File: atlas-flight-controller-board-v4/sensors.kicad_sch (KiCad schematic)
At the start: 14 parts, among them IC1 LSM6DSV80XTR, U2 LIS2MDL, U3 SAM-M10Q-00B

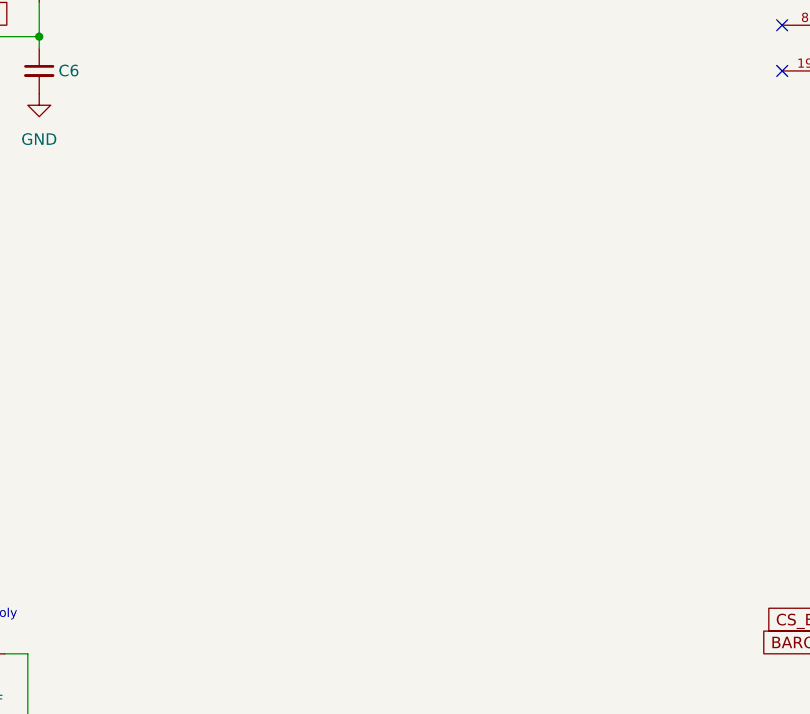
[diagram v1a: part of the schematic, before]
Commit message: commiting files to v10 branch. Only v9 is working well on linux so seperating to reduce headache while sorting out issues
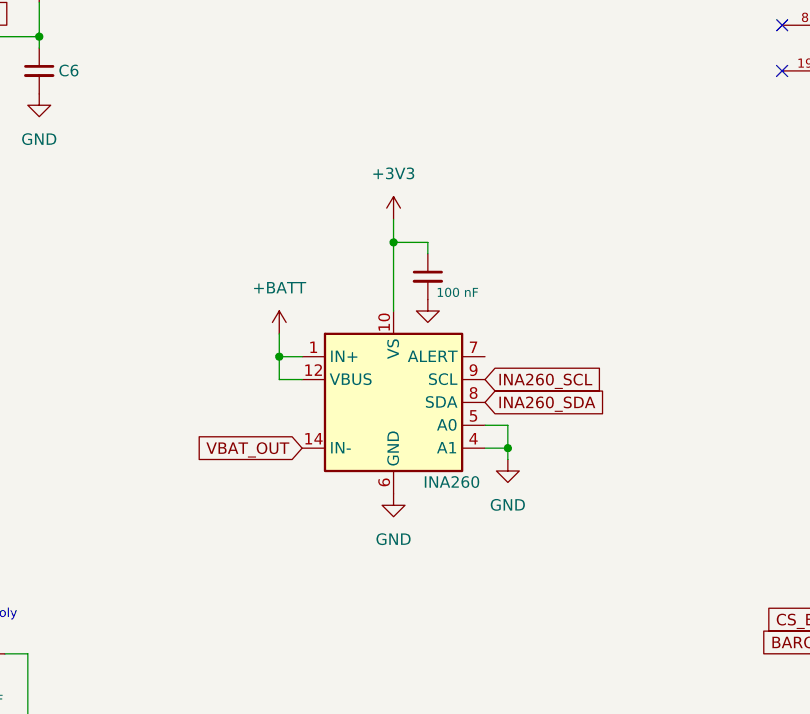
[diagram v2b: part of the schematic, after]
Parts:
- added C27: 100 nF, Capacitor_SMD:C_0603_1608Metric_Pad1.08x0.95mm_HandSolder, symbol Device:C_Small
- added U5: INA260, Package_SO:TSSOP-16_4.4x5mm_P0.65mm, symbol Sensor_Energy:INA260
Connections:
- net +3V3: now also C27.1, U5.10 (VS)
- net GND: now also C27.2, U5.11 (GND), U5.4 (A1), U5.5 (A0), U5.6 (GND)
- new net +BATT: U5.1 (IN+), U5.12 (VBUS), U5.2 (IN+), U5.3 (IN+)
- new net INA260_SCL: U5.9 (SCL)
- new net INA260_SDA: U5.8 (SDA)
- new net VBAT_OUT: U5.14 (IN-), U5.15 (IN-), U5.16 (IN-)

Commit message: wip commit, hopefully last from mac
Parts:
- removed C1: 10 uF, CAP_APA_0606_AVX, symbol APA0606100M050R:_1
- added C43: 10uF, Capacitor_SMD:C_0603_1608Metric, symbol Device:C_Small
- C10, C27, C5, C6, C7, C8, C9: footprint Capacitor_SMD:C_0603_1608Metric_Pad1.08x0.95mm_HandSolder -> Capacitor_SMD:C_0603_1608Metric
- C2, C3: value 100 nF -> 100nF; footprint Capacitor_SMD:C_0603_1608Metric_Pad1.08x0.95mm_HandSolder -> Capacitor_SMD:C_0603_1608Metric
- C4: value 220 nF -> 220nF; footprint Capacitor_SMD:C_0603_1608Metric_Pad1.08x0.95mm_HandSolder -> Capacitor_SMD:C_0603_1608Metric
- U2: footprint LIS2MDL:PQFN50P200X200X70-12N -> Package_LGA:LGA-12_2x2mm_P0.5mm
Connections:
- net +3V3: now also C43.2
- net GND: now also C43.1
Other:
- note removed: "Alum Poly"
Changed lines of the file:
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@@
 	(generator_version "10.0")
 	(paper "A4")
-	(text "Alum Poly\n"
-		(exclude_from_sim no)
-		(at 99.568 127.762 0)
-		(effects
-			(font
-				(size 1 1)
-			)
-		)
-	)
 	(junction
 		(at 76.2 81.28)
@@
 	(wire
 		(pts
-			(xy 49.53 160.02) (xy 50.8 160.02)
-		)
-		(stroke
-			(width 0)
-			(type default)
-		)
-	)
-	(wire
-		(pts
 			(xy 39.37 62.23) (xy 39.37 60.96)
 		)
@@
 	(wire
 		(pts
-			(xy 49.53 157.48) (xy 50.8 157.48)
-		)
-		(stroke
-			(width 0)
-			(type default)
-		)
-	)
-	(wire
-		(pts
 			(xy 246.38 130.81) (xy 250.19 130.81)
 		)
@@
 	(wire
 		(pts
-			(xy 49.53 152.4) (xy 50.8 152.4)
-		)
-		(stroke
-			(width 0)
-			(type default)
-		)
-	)
-	(wire
-		(pts
 			(xy 95.25 132.08) (xy 96.52 132.08)
 		)
@@
 	(global_label "SCK_MEMS"
 		(shape input)
-		(at 49.53 152.4 180)
+		(at 50.8 152.4 180)
 		(fields_autoplaced yes)
 		(effects
@@
 		)
 		(property "Intersheetrefs" "${INTERSHEET_REFS}"
-			(at 36.5664 152.4 0)
+			(at 37.8364 152.4 0)
 			(hide yes)
 			(show_name no)
@@
 	(global_label "MISO_MEMS"
 		(shape input)
-		(at 49.53 160.02 180)
+		(at 50.8 160.02 180)
 		(fields_autoplaced yes)
 		(effects
@@
 		)
 		(property "Intersheetrefs" "${INTERSHEET_REFS}"
-			(at 35.7197 160.02 0)
+			(at 36.9897 160.02 0)
 			(hide yes)
 			(show_name no)
@@
 	(global_label "MOSI_MEMS"
 		(shape input)
-		(at 49.53 157.48 180)
+		(at 50.8 157.48 180)
 		(fields_autoplaced yes)
 		(effects
@@
 		)
 		(property "Intersheetrefs" "${INTERSHEET_REFS}"
-			(at 35.7197 157.48 0)
+			(at 36.9897 157.48 0)
 			(hide yes)
 			(show_name no)
@@
 			)
 		)
-		(property "Value" "100 nF"
+		(property "Value" "100nF"
 			(at 99.06 137.16 90)
 			(show_name no)
@@
 			)
 		)
-		(property "Footprint" "Capacitor_SMD:C_0603_1608Metric_Pad1.08x0.95mm_HandSolder"
+		(property "Footprint" "Capacitor_SMD:C_0603_1608Metric"
 			(at 99.06 139.7 0)
 			(hide yes)
@@
 			)
 		)
-		(property "Footprint" "Capacitor_SMD:C_0603_1608Metric_Pad1.08x0.95mm_HandSolder"
+		(property "Footprint" "Capacitor_SMD:C_0603_1608Metric"
 			(at 243.84 124.46 0)
 			(hide yes)
@@
 			)
 		)
-		(property "Footprint" "Capacitor_SMD:C_0603_1608Metric_Pad1.08x0.95mm_HandSolder"
+		(property "Footprint" "Capacitor_SMD:C_0603_1608Metric"
 			(at 238.76 52.07 0)
 			(hide yes)
@@
 			)
 		)
-		(property "Value" "100 nF"
+		(property "Value" "100nF"
 			(at 99.314 144.78 90)
 			(show_name no)
@@
 			)
 		)
-		(property "Footprint" "Capacitor_SMD:C_0603_1608Metric_Pad1.08x0.95mm_HandSolder"
+		(property "Footprint" "Capacitor_SMD:C_0603_1608Metric"
 			(at 99.06 147.32 0)
 			(hide yes)
@@
 	)
 	(symbol
-		(lib_id "APA0606100M050R:_1")
-		(at 99.06 129.54 0)
-		(unit 1)
-		(body_style 1)
-		(exclude_from_sim no)
-		(in_bom yes)
-		(on_board yes)
-		(in_pos_files yes)
-		(dnp no)
-		(property "Reference" "C1"
-			(at 102.87 123.19 0)
-			(hide yes)
-			(show_name no)
-			(do_not_autoplace no)
-			(effects
-				(font
-					(size 1.524 1.524)
-				)
-			)
-		)
-		(property "Value" "10 uF"
-			(at 99.06 129.54 0)
-			(show_name no)
-			(do_not_autoplace no)
-			(effects
-				(font
-					(size 1 1)
-				)
-			)
-		)
-		(property "Footprint" "CAP_APA_0606_AVX"
-			(at 99.06 129.54 0)
-			(hide yes)
-			(show_name no)
-			(do_not_autoplace no)
-			(effects
-				(font
-					(size 1.27 1.27)
-				)
-			)
-		)
-		(property "Datasheet" "APA0606100M050R"
-			(at 99.06 129.54 0)
-			(hide yes)
-			(show_name no)
-			(do_not_autoplace no)
-			(effects
-				(font
-					(size 1.27 1.27)
-				)
-			)
-		)
-		(property "Description" ""
-			(at 99.06 129.54 0)
-			(hide yes)
-			(show_name no)
-			(do_not_autoplace no)
-			(effects
-				(font
-					(size 1.27 1.27)
-				)
-			)
-		)
-		(pin "1"
-		)
-		(pin "2"
-		)
-		(instances
-			(project "atlas-flight-controller-board-v4"
-				(path "/5e529273-3bf8-4f62-b3e5-dd579b5c7f6d/d2d48602-e6ee-4bc4-bdea-4cc645152de4"
-					(reference "C1")
-					(unit 1)
-				)
-			)
-			(project "atlas-flight-controller-board"
-				(path "/99efb2d6-b5f7-438c-9ed2-f359400f01a1/5584e1ef-6e93-420a-9bdf-15a5926ce2b3"
-					(reference "C3")
-					(unit 1)
-				)
-			)
-		)
-	)
-	(symbol
 		(lib_id "power:GND")
 		(at 39.37 62.23 0)
@@
 			)
 		)
-		(property "Footprint" "Capacitor_SMD:C_0603_1608Metric_Pad1.08x0.95mm_HandSolder"
+		(property "Footprint" "Capacitor_SMD:C_0603_1608Metric"
 			(at 73.66 85.09 0)
 			(hide yes)
@@
 			)
 		)
-		(property "Footprint" "LIS2MDL:PQFN50P200X200X70-12N"
+		(property "Footprint" "Package_LGA:LGA-12_2x2mm_P0.5mm"
 			(at 71.12 154.94 0)
 			(hide yes)
@@
 			)
 		)
-		(property "Footprint" "Capacitor_SMD:C_0603_1608Metric_Pad1.08x0.95mm_HandSolder"
+		(property "Footprint" "Capacitor_SMD:C_0603_1608Metric"
 			(at 243.84 130.81 0)
 			(hide yes)
@@
 			)
 		)
-		(property "Footprint" "Capacitor_SMD:C_0603_1608Metric_Pad1.08x0.95mm_HandSolder"
+		(property "Footprint" "Capacitor_SMD:C_0603_1608Metric"
 			(at 250.19 52.07 0)
 			(hide yes)
@@
 			)
 		)
-		(property "Footprint" "Capacitor_SMD:C_0603_1608Metric_Pad1.08x0.95mm_HandSolder"
+		(property "Footprint" "Capacitor_SMD:C_0603_1608Metric"
 			(at 105.41 67.31 0)
 			(hide yes)
@@
 			)
 		)
-		(property "Value" "220 nF"
+		(property "Value" "220nF"
 			(at 96.774 156.972 90)
 			(show_name no)
@@
 			)
 		)
-		(property "Footprint" "Capacitor_SMD:C_0603_1608Metric_Pad1.08x0.95mm_HandSolder"
+		(property "Footprint" "Capacitor_SMD:C_0603_1608Metric"
 			(at 99.06 152.4 0)
 			(hide yes)
@@
 	)
 	(symbol
+		(lib_id "Device:C_Small")
+		(at 99.06 132.08 270)
+		(unit 1)
+		(body_style 1)
+		(exclude_from_sim no)
+		(in_bom yes)
+		(on_board yes)
+		(in_pos_files yes)
+		(dnp no)
+		(property "Reference" "C43"
+			(at 99.0536 125.73 90)
+			(hide yes)
+			(show_name no)
+			(do_not_autoplace no)
+			(effects
+				(font
+					(size 1.27 1.27)
+				)
+			)
+		)
+		(property "Value" "10uF"
+			(at 99.06 129.54 90)
+			(show_name no)
+			(do_not_autoplace no)
+			(effects
+				(font
+					(size 1 1)
+				)
+			)
+		)
+		(property "Footprint" "Capacitor_SMD:C_0603_1608Metric"
+			(at 99.06 132.08 0)
+			(hide yes)
+			(show_name no)
+			(do_not_autoplace no)
+			(effects
+				(font
+					(size 1.27 1.27)
+				)
+			)
+		)
+		(property "Datasheet" ""
+			(at 99.06 132.08 0)
+			(hide yes)
+			(show_name no)
+			(do_not_autoplace no)
+			(effects
+				(font
+					(size 1.27 1.27)
+				)
+			)
+		)
+		(property "Description" "Unpolarized capacitor, small symbol"
+			(at 99.06 132.08 0)
+			(hide yes)
+			(show_name no)
+			(do_not_autoplace no)
+			(effects
+				(font
+					(size 1.27 1.27)
+				)
+			)
+		)
+		(pin "2"
+		)
+		(pin "1"
+		)
+		(instances
+			(project "atlas-flight-controller-board-v4"
+				(path "/5e529273-3bf8-4f62-b3e5-dd579b5c7f6d/d2d48602-e6ee-4bc4-bdea-4cc645152de4"
+					(reference "C43")
+					(unit 1)
+				)
+			)
+		)
+	)
+	(symbol
 		(lib_id "power:+3V3")
 		(at 238.76 116.84 0)
@@
 			)
 		)
-		(property "Footprint" "Capacitor_SMD:C_0603_1608Metric_Pad1.08x0.95mm_HandSolder"
+		(property "Footprint" "Capacitor_SMD:C_0603_1608Metric"
 			(at 148.59 90.17 0)
 			(hide yes)
@@
 		)
 	)
+	(group "LIS2MDL_SPI"
+		(lib_id "sensors:LIS2MDL_SPI")
+		(members "0ab791aa-7cbb-4318-bc85-4e8e8c9142c7" "0cae57a6-3bdc-49c7-b001-25d194668baa"
+			"0da27fe1-ef6c-4f5f-8832-551961ca739f" "1085d7a7-3055-4f5f-9ba4-95fcd3dd7744"
+			"117e3f07-91ac-4877-9d0d-a8e8ae910851" "1345939e-8d55-4c78-9438-36bc38fe63d8"
+			"20e6a362-2413-45e7-8593-fe80701a17db" "23818bd5-0043-4d40-8233-e253ec623bdb"
+			"397bee4b-c0a1-46e5-a201-1a473b300a2c" "3b12599e-31d8-4be3-82ba-776ebb0edcdb"
+			"3c1f30ef-fab7-4d20-85c3-e40c0ceea278" "487c97c7-788f-4e6c-a4bf-7b4fc57dd327"
+			"48feaa2d-7542-4848-b2f6-2a4188d77647" "4ccd61d2-3aae-4863-af96-72e30f40c39d"
+			"50e5cc8d-390a-4e7b-bf1d-298a2fee927b" "5d645774-8ede-4a1f-ac11-8c02df5791f6"
+			"5eca3add-a6a8-46dd-9c30-d522ade3a89b" "7edb4f66-e049-4758-9f3e-1b64f01c0ab9"
+			"8051ba19-5127-478b-bcd1-e87c78e954af" "927fdbf8-3c3e-4d01-9dec-d4773c8cd34e"
+			"96ca15d9-9f17-4c57-9eaf-5d222d5ebc0b" "98d0a383-107f-48bc-bfaa-667d4aa1a20b"
+			"9c4634bb-ea80-4714-a8c2-e105f84e44be" "9cf5a10a-49fa-4109-b221-99e2d35aa729"
+			"a36e8ce5-9247-4f58-ab08-8e2bafe2dd36" "aa6397bc-1037-4031-81ff-7dfde0e412eb"
+			"ac8b1d57-ce24-49c4-bca9-bfca44e9c67f" "ba29355b-5ef9-4ffb-b129-3825cd0082a9"
+			"bbc780eb-e731-451e-84b1-d9695948ab0d" "bc82a8d2-0c1f-4e70-ae0a-219a7db42c13"
+			"bca47364-4c82-456c-8a0f-f63c8a29ea21" "bf30be68-2d0a-45cd-99a1-bbfbfe76de56"
+			"c028be64-9e7a-4d01-a29b-66698c2836a4" "c0d602bb-fbb3-4c74-bbbd-22a55f8ccb4d"
+			"c141713b-3189-4866-b5eb-c6fa5cbbb8b2" "c5a55356-2dbf-4121-92d1-e403ace39fac"
+			"d531354f-63c9-44b6-9698-2df9d2b522bf" "dc9c2fec-777b-449b-a278-69c0931d7768"
+			"e2e8ed59-7e93-4b7b-9bf1-fa7561fee952" "f40ad0f8-f820-4b89-8a1c-e228ed56d6cf"
+			"faa480ac-9035-4bc3-b485-3816ef265dc4" "fbeca2d6-bb8c-405e-a48d-a725f675466f"
+		)
+	)

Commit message: schematic done mostly besides style and footprints
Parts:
- C1: renamed from C9; footprint Capacitor_SMD:C_0603_1608Metric -> Capacitor_SMD:C_0402_1005Metric
- C10: renamed from C3; footprint Capacitor_SMD:C_0603_1608Metric -> Capacitor_SMD:C_0402_1005Metric
- C11: renamed from C4; footprint Capacitor_SMD:C_0603_1608Metric -> Capacitor_SMD:C_0402_1005Metric
- C2: renamed from C10; footprint Capacitor_SMD:C_0603_1608Metric -> Capacitor_SMD:C_0402_1005Metric
- C3: renamed from C6; footprint Capacitor_SMD:C_0603_1608Metric -> Capacitor_SMD:C_0402_1005Metric
- C4: renamed from C5; footprint Capacitor_SMD:C_0603_1608Metric -> Capacitor_SMD:C_0402_1005Metric
- C5: renamed from C27; footprint Capacitor_SMD:C_0603_1608Metric -> Capacitor_SMD:C_0402_1005Metric
- C6: renamed from C7; footprint Capacitor_SMD:C_0603_1608Metric -> Capacitor_SMD:C_0402_1005Metric
- C7: renamed from C8; footprint Capacitor_SMD:C_0603_1608Metric -> Capacitor_SMD:C_0402_1005Metric
- C9: renamed from C2; footprint Capacitor_SMD:C_0603_1608Metric -> Capacitor_SMD:C_0402_1005Metric
- renumbered C43 to C8, U3 to U1, U5 to U2, U2 to U3
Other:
- company: (none) -> Sam Manley, ARCUIA
- title: (none) -> Atlas v4 Flight Controller

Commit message: progress update. schematic has been done, layout is half finished. board is now 50x65mm for rf performance reasons
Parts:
- C17: renamed from C1; value 0.1uF -> 100n
- C18: renamed from C2; value 0.1uF -> 100n
- C19: renamed from C3; value 100 nF -> 100n
- C20: renamed from C4; value 100 nF -> 100n
- C21: renamed from C5; value 100 nF -> 100n
- C22: renamed from C6; value 100 nF -> 100n
- C23: renamed from C7; value 100 nF -> 100n
- C24: renamed from C8; value 10uF -> 10u
- C25: renamed from C9; value 100nF -> 100n
- C26: renamed from C10; value 100nF -> 100n
- C27: renamed from C11; value 220nF -> 220n
- renumbered U1 to U4, U2 to U5, U3 to U6
